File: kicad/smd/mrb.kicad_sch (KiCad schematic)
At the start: 9 parts

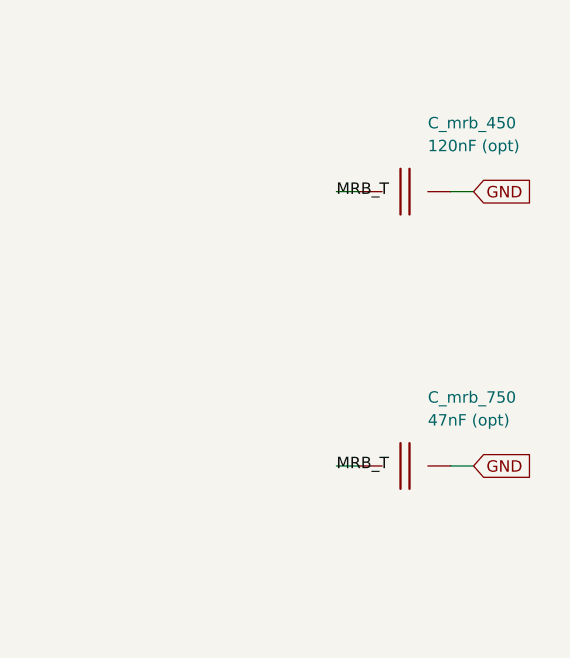
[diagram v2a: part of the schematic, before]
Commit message: Noise, hum, crosstalk and thermal models; three design fixes; JLCPCB rules and cost
New models (docs/06c, spice/): a .noise run of the whole front end including the
LM317's own rail noise, the rail-ripple paths to the speaker, a vactrol-level tremolo
depth model, an electro-thermal LM1875 ladder, and a geometric crosstalk audit of the
routed boards (kicad/gen/crosstalk_audit.py). They found three defects:

- Errata #21 (hum + hiss): the LM1875 bias divider had no bypass (+4 dB ripple to
  speaker, 0.4 Vrms of 100 Hz at idle) and the LM317's 0.5 mV of noise reached the
  0 dB-PSRR JFET stages (23 dB above their floor, SNR 34 dB). Fixed with C_bref +
  R_bias3 on the power amp, C_adj on the regulator, and an RC-decoupled +17V_PRE rail
  for Q1/Q2/Q_rec: hum 408 mV -> 0.3 mV, EIN 37 -> 2.7 uV, SNR 34 -> 57 dB.
- Errata #22 (tremolo depth 1.7 dB): the vactrol LED was returned to ground from a
  mid-rail LFO -> 7 mA DC, a fixed -20 dB pad. LED limiter (2 V swing, LED_rate is one
  limiter LED) + Q_trem 2N3904/MMBT3904 emitter follower AC-coupled from the depth
  pot -> 15 dB depth, 0.8 dB insertion loss.
- Errata #23 (fab): stock TO-92 and the LM1875 footprint were under JLCPCB's 0.18 mm
  annular-ring minimum -> TO-92_Inline_Wide and 1.5 mm LM1875 pads; both .kicad_pro
  carry JLC's 2-layer limits as DRC constraints. Cost: all SMD caps 1206 (basic
  library), "(opt)" MRB caps DNP, gyrator on E24 values (same 1.86 H): 7 -> 2
  extended part types, ~$32 -> ~$17 assembly for five boards (kicad/gen/jlc_cost.py);
  three fiducials on the SMD board.

Crosstalk -> two routing rules (.kicad_dru: HighCurrent 0.6/0.4 mm and TankDrive
1.2/0.8 mm from signal copper, THT/SMD) that route_board.py also hands the router as
class clearances; keepout rule areas along the edge and around the mounting holes.
Thermal: Part 5's <= 2.5 K/W heatsink confirmed with numbers (Tj 97 C at 40 C ambient,
worst-case sine; 8-10 K/W clip-ons reach shutdown).

Placer: short parts stack beside tall ones i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
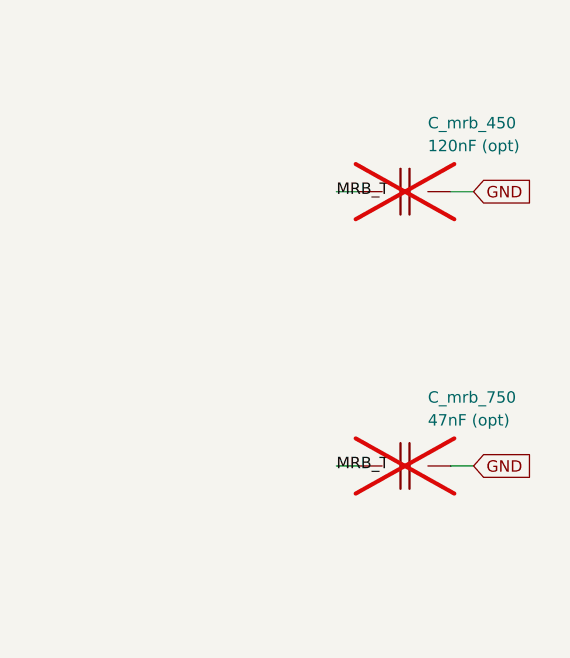
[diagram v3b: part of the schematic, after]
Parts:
- C_mrb_450: footprint Capacitor_SMD:C_1210_3225Metric -> Capacitor_SMD:C_1206_3216Metric; now not fitted
- C_mrb_750: now not fitted
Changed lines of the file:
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@@
     (pin "1")
     (pin "2")
-    (instances (project "cambridge_reverb" (path "/ec912737-e97f-491f-b380-fa898b594446" (reference "C_mrb_in") (unit 1))))
+    (instances (project "cambridge_reverb" (path "/bc7c1aa7-b119-440e-9500-529c21fc3222" (reference "C_mrb_in") (unit 1))))
   )
   (wire (pts (xy 146.05 48.25999999999999) (xy 143.51 48.25999999999999)) (stroke (width 0) (type default)))
@@
     (pin "1")
     (pin "2")
-    (instances (project "cambridge_reverb" (path "/ec912737-e97f-491f-b380-fa898b594446" (reference "R_mrb_ser") (unit 1))))
+    (instances (project "cambridge_reverb" (path "/bc7c1aa7-b119-440e-9500-529c21fc3222" (reference "R_mrb_ser") (unit 1))))
   )
   (wire (pts (xy 186.69 48.25999999999999) (xy 184.14999999999998 48.25999999999999)) (stroke (width 0) (type default)))
@@
     (pin "1")
     (pin "2")
-    (instances (project "cambridge_reverb" (path "/ec912737-e97f-491f-b380-fa898b594446" (reference "L1") (unit 1))))
+    (instances (project "cambridge_reverb" (path "/bc7c1aa7-b119-440e-9500-529c21fc3222" (reference "L1") (unit 1))))
   )
   (wire (pts (xy 226.06 78.74) (xy 223.51999999999998 78.74)) (stroke (width 0) (type default)))
@@
     (pin "1")
     (pin "2")
-    (instances (project "cambridge_reverb" (path "/ec912737-e97f-491f-b380-fa898b594446" (reference "C_mrb_600") (unit 1))))
+    (instances (project "cambridge_reverb" (path "/bc7c1aa7-b119-440e-9500-529c21fc3222" (reference "C_mrb_600") (unit 1))))
   )
   (wire (pts (xy 266.7 78.74) (xy 264.15999999999997 78.74)) (stroke (width 0) (type default)))
@@
   (global_label "GND" (shape input) (at 279.4 78.74 0) (fields_autoplaced) (effects (font (size 1.27 1.27)) (justify left)))
   (symbol (lib_id "cr_primitives:C") (at 271.78 107.94999999999999 0) (unit 1)
-    (in_bom yes) (on_board yes) (dnp no)
+    (in_bom yes) (on_board yes) (dnp yes)
     (property "Reference" "C_mrb_450" (at 274.32 100.32999999999998 0) (effects (font (size 1.27 1.27)) (justify left)))
     (property "Value" "120nF (opt)" (at 274.32 102.86999999999999 0) (effects (font (size 1.27 1.27)) (justify left)))
-    (property "Footprint" "Capacitor_SMD:C_1210_3225Metric" (at 271.78 107.94999999999999 0) (effects (font (size 1.27 1.27)) hide))
+    (property "Footprint" "Capacitor_SMD:C_1206_3216Metric" (at 271.78 107.94999999999999 0) (effects (font (size 1.27 1.27)) hide))
     (pin "1")
     (pin "2")
-    (instances (project "cambridge_reverb" (path "/ec912737-e97f-491f-b380-fa898b594446" (reference "C_mrb_450") (unit 1))))
+    (instances (project "cambridge_reverb" (path "/bc7c1aa7-b119-440e-9500-529c21fc3222" (reference "C_mrb_450") (unit 1))))
   )
   (wire (pts (xy 266.7 107.94999999999999) (xy 264.15999999999997 107.94999999999999)) (stroke (width 0) (type default)))
@@
   (global_label "GND" (shape input) (at 279.4 107.94999999999999 0) (fields_autoplaced) (effects (font (size 1.27 1.27)) (justify left)))
   (symbol (lib_id "cr_primitives:C") (at 271.78 138.43 0) (unit 1)
-    (in_bom yes) (on_board yes) (dnp no)
+    (in_bom yes) (on_board yes) (dnp yes)
     (property "Reference" "C_mrb_750" (at 274.32 130.81 0) (effects (font (size 1.27 1.27)) (justify left)))
     (property "Value" "47nF (opt)" (at 274.32 133.35 0) (effects (font (size 1.27 1.27)) (justify left)))
@@
     (pin "1")
     (pin "2")
-    (instances (project "cambridge_reverb" (path "/ec912737-e97f-491f-b380-fa898b594446" (reference "C_mrb_750") (unit 1))))
+    (instances (project "cambridge_reverb" (path "/bc7c1aa7-b119-440e-9500-529c21fc3222" (reference "C_mrb_750") (unit 1))))
   )
   (wire (pts (xy 266.7 138.43) (xy 264.15999999999997 138.43)) (stroke (width 0) (type default)))
@@
     (pin "1")
     (pin "2")
-    (instances (project "cambridge_reverb" (path "/ec912737-e97f-491f-b380-fa898b594446" (reference "C_mrb_out") (unit 1))))
+    (instances (project "cambridge_reverb" (path "/bc7c1aa7-b119-440e-9500-529c21fc3222" (reference "C_mrb_out") (unit 1))))
   )
   (wire (pts (xy 186.69 107.94999999999999) (xy 184.14999999999998 107.94999999999999)) (stroke (width 0) (type default)))
@@
     (pin "1")
     (pin "2")
-    (instances (project "cambridge_reverb" (path "/ec912737-e97f-491f-b380-fa898b594446" (reference "R_fs_mrb") (unit 1))))
+    (instances (project "cambridge_reverb" (path "/bc7c1aa7-b119-440e-9500-529c21fc3222" (reference "R_fs_mrb") (unit 1))))
   )
   (wire (pts (xy 146.05 138.43) (xy 143.51 138.43)) (stroke (width 0) (type default)))
@@
     (property "Footprint" "cambridge_reverb:TestPoint_THT_D2.0mm_Label" (at 140.97 228.6 0) (effects (font (size 1.27 1.27)) hide))
     (pin "1")
-    (instances (project "cambridge_reverb" (path "/ec912737-e97f-491f-b380-fa898b594446" (reference "TP_MRB_OUT") (unit 1))))
+    (instances (project "cambridge_reverb" (path "/bc7c1aa7-b119-440e-9500-529c21fc3222" (reference "TP_MRB_OUT") (unit 1))))
   )
   (wire (pts (xy 140.97 231.14) (xy 140.97 233.67999999999998)) (stroke (width 0) (type default)))
